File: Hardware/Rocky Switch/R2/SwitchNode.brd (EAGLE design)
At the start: 67.1 x 45.7 mm, 28 parts, among them T1 2SC1815, T2 2SC1815, T3 C1815

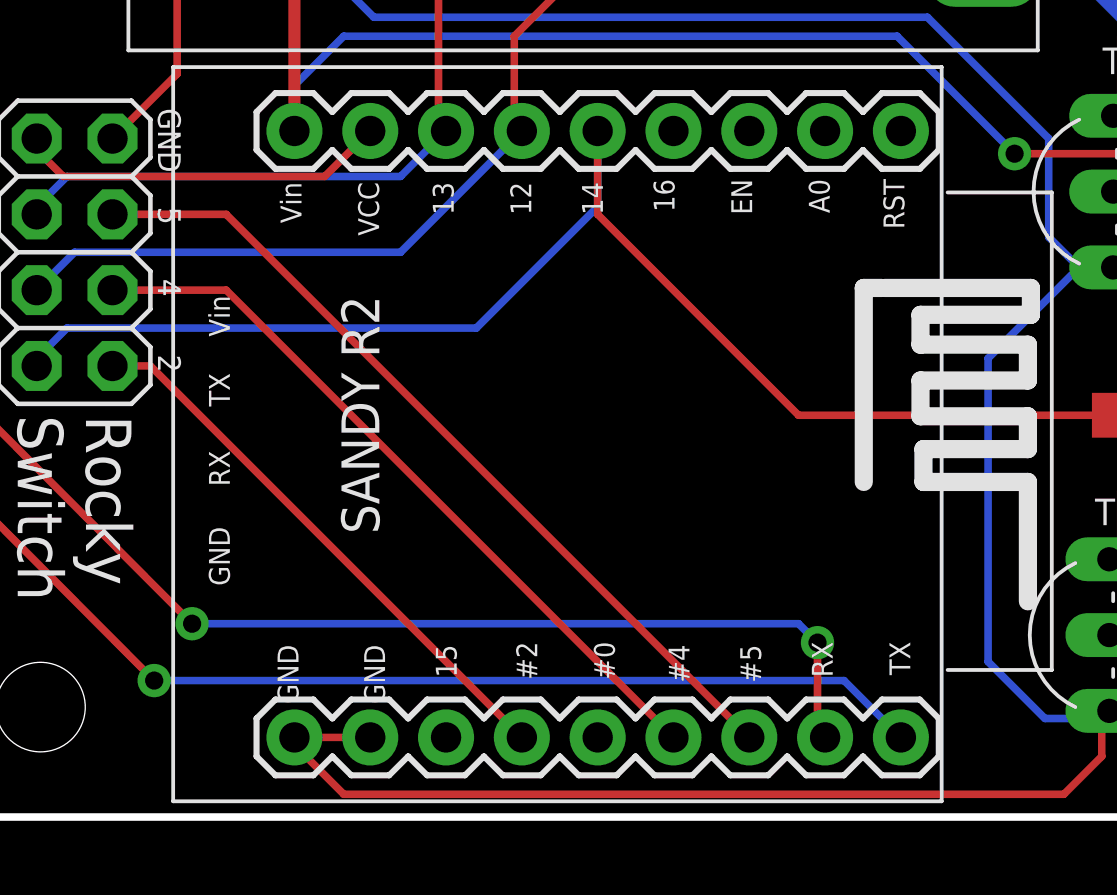
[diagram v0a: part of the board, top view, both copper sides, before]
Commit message: Rename SwitchNode to Rocky Switch and change to use Wemos D1 Mini
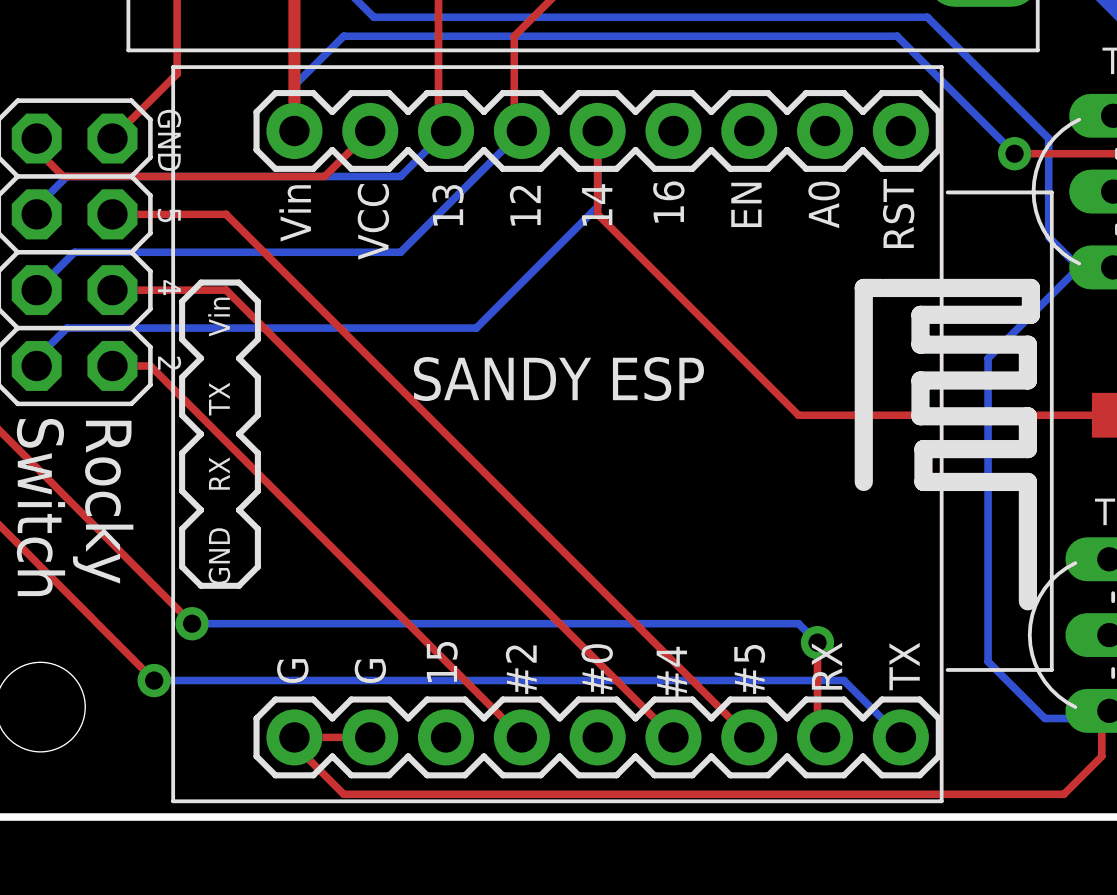
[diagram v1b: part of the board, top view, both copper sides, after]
